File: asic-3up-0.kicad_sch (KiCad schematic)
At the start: 81 parts, among them U10 BM1362AC_MODE1, U12 MCP1824T-1202E/OT, U13 MCP1824T-0802E, U14 MCP1824T-1202E/OT, U15 MCP1824T-0802E, U4 MCP1824T-1202E/OT, U5 MCP1824T-0802E, U8 BM1362AC_MODE1, U9 BM1362AC_MODE0

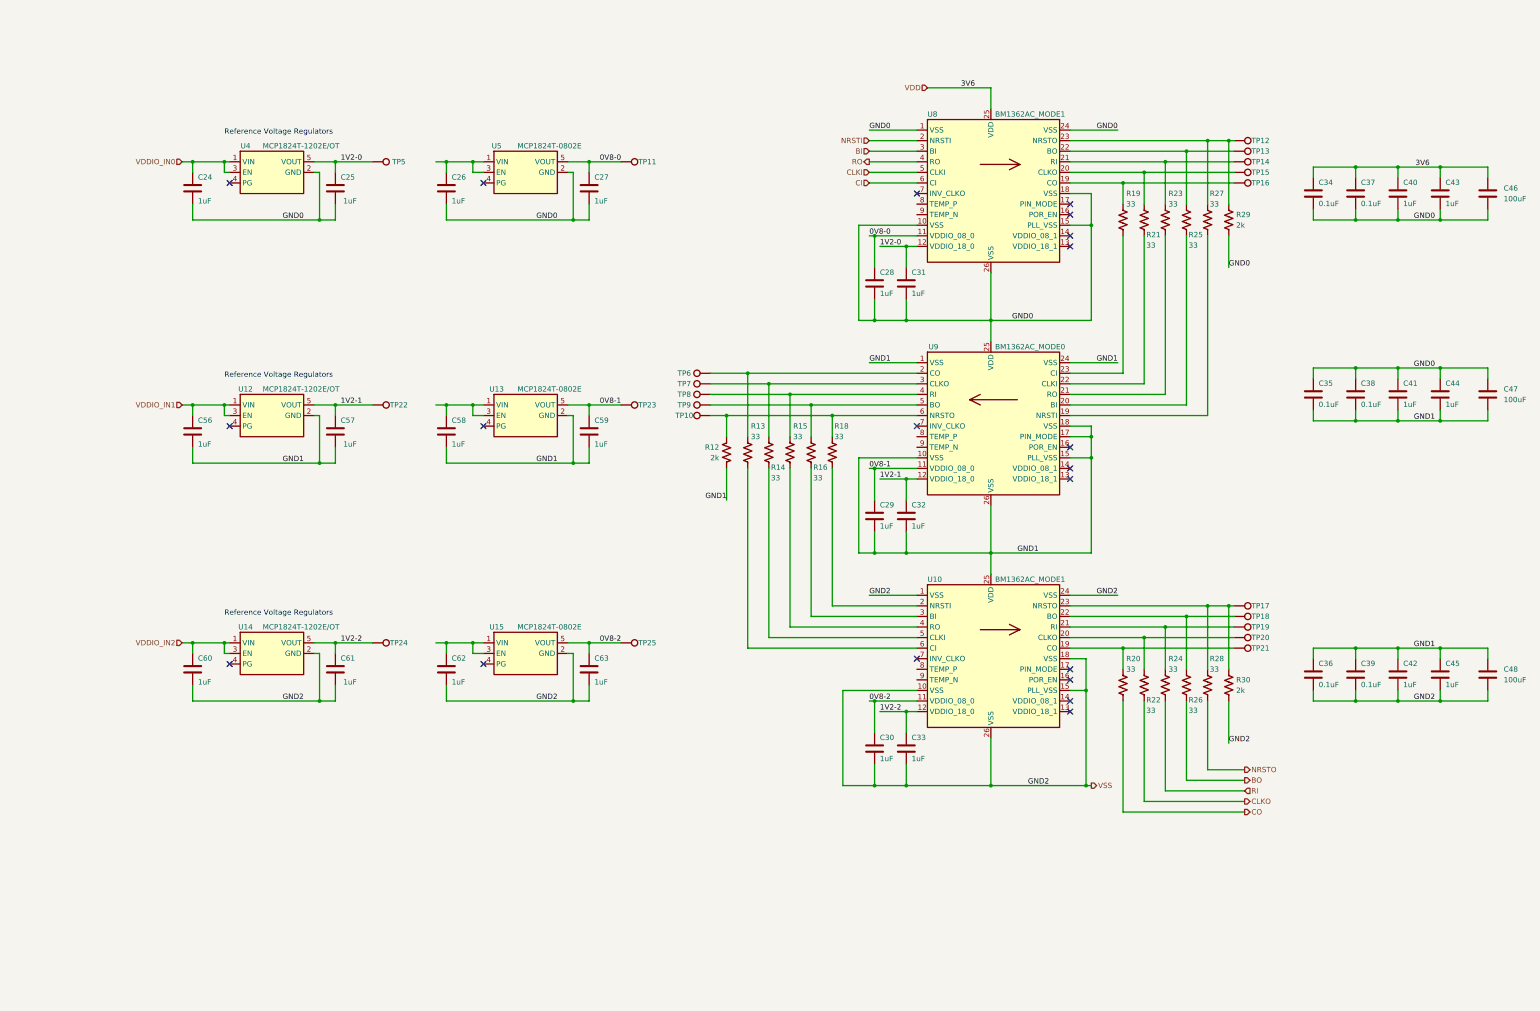
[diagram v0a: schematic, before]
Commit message: added all the ASICs to the schematic. added the RP2040 circuit for data. added the VDDIO boost circuit. schematic cleanup
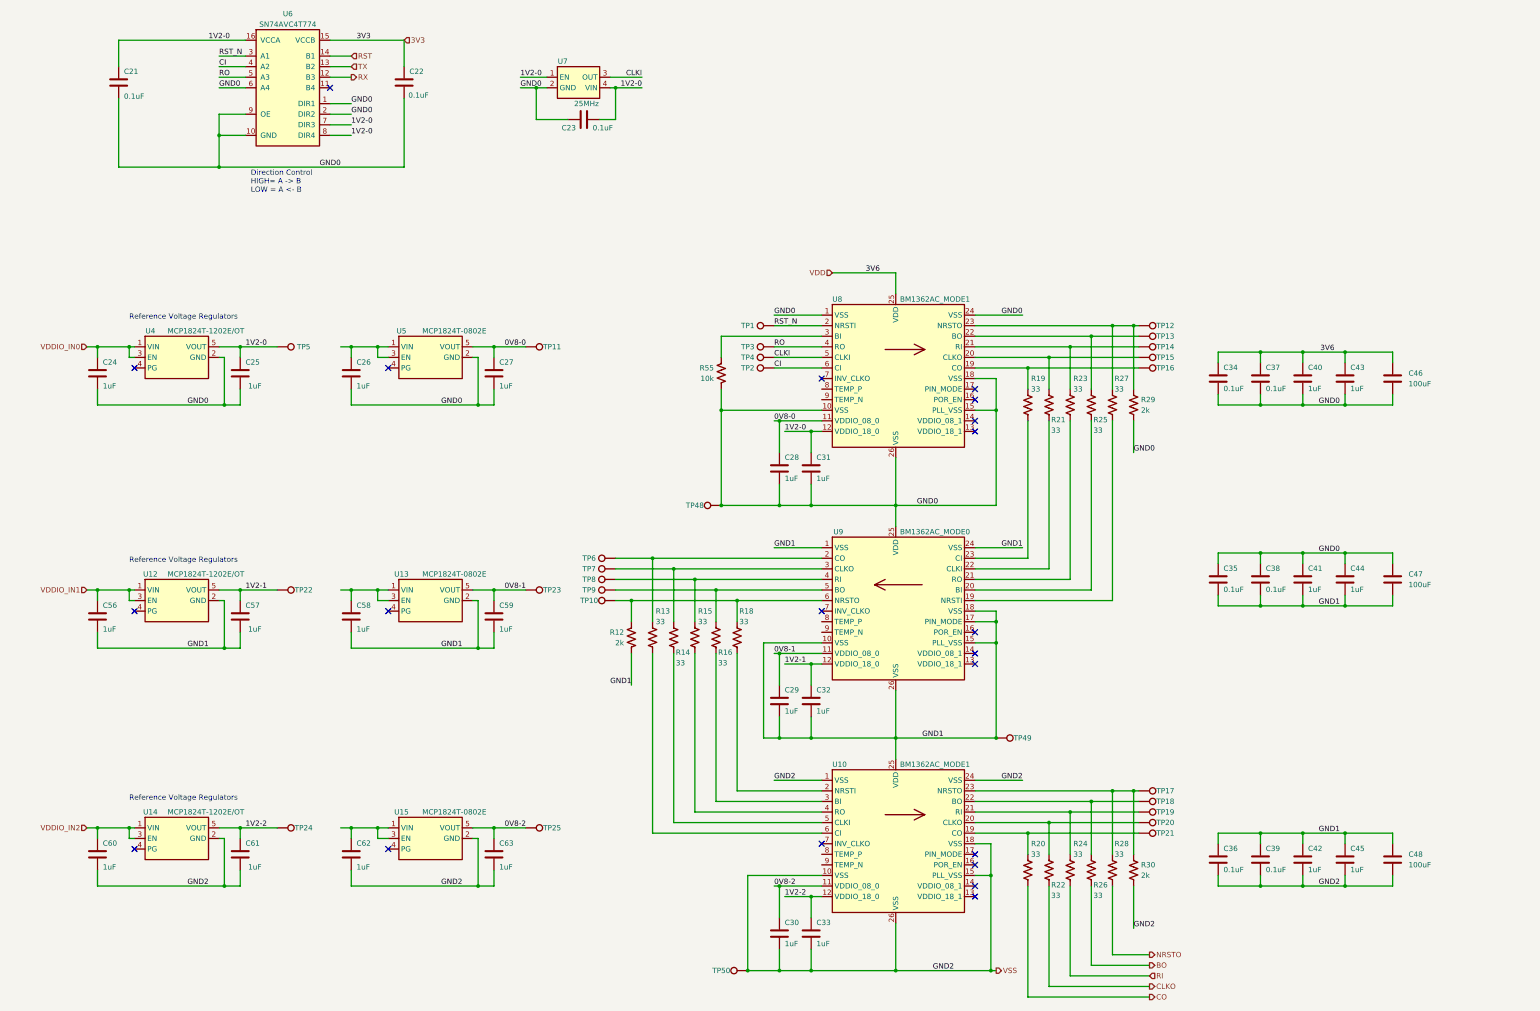
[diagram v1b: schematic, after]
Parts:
- added C21, C22, C23: 0.1uF, Capacitor_SMD:C_0402_1005Metric, symbol Device:C
- added R55: 10k, Resistor_SMD:R_0402_1005Metric, symbol Device:R_US
- added TP1, TP2, TP3, TP4, TP48, TP49, TP50: TestPoint, TestPoint:TestPoint_Pad_D1.5mm, symbol Connector:TestPoint
- added U6: SN74AVC4T774, Package_SO:TSSOP-16_4.4x5mm_P0.65mm, symbol bitaxe:SN74AVC4T774
- added U7: 25MHz, bitaxe:SMD3225-4P, symbol bitaxe:oscillator
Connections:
- net 1V2-0: now also C21.1, C23.2, U6.16 (VCCA), U6.7 (DIR3), U6.8 (DIR4), U7.1 (EN), U7.4 (VIN)
- net CI: now also TP2.1, U6.4 (A2)
- net CLKI: now also TP4.1, U7.3 (OUT)
- net GND0: now also C21.2, C22.2, C23.1, R55.2, TP48.1, U6.1 (DIR1), U6.10 (GND), U6.2 (DIR2), U6.6 (A4), U6.9 (OE), U7.2 (GND)
- net GND1: now also TP49.1
- net RO: now also TP3.1, U6.5 (A3)
- net VSS: now also TP50.1
- net BI: no longer names the net of U8.3 (BI)
- net BI: now also R55.1
- net NRSTI renamed RST_N
- net RST_N: now also TP1.1, U6.3 (A1)
- new net 3V3: C22.1, U6.15 (VCCB)
- new net RST: U6.14 (B1)
- new net RX: U6.12 (B3)
- new net TX: U6.13 (B2)
- no-connect marks 20 -> 21
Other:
- note added: "Direction Control HIGH= A -> B LOW = A <- B"
- moved on the sheet: C24, C25, C26, C27, C28, C29, C30, C31, C32, C33, C34, C35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

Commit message: added sweet logo to schematic worksheet. Schematic cleanup.
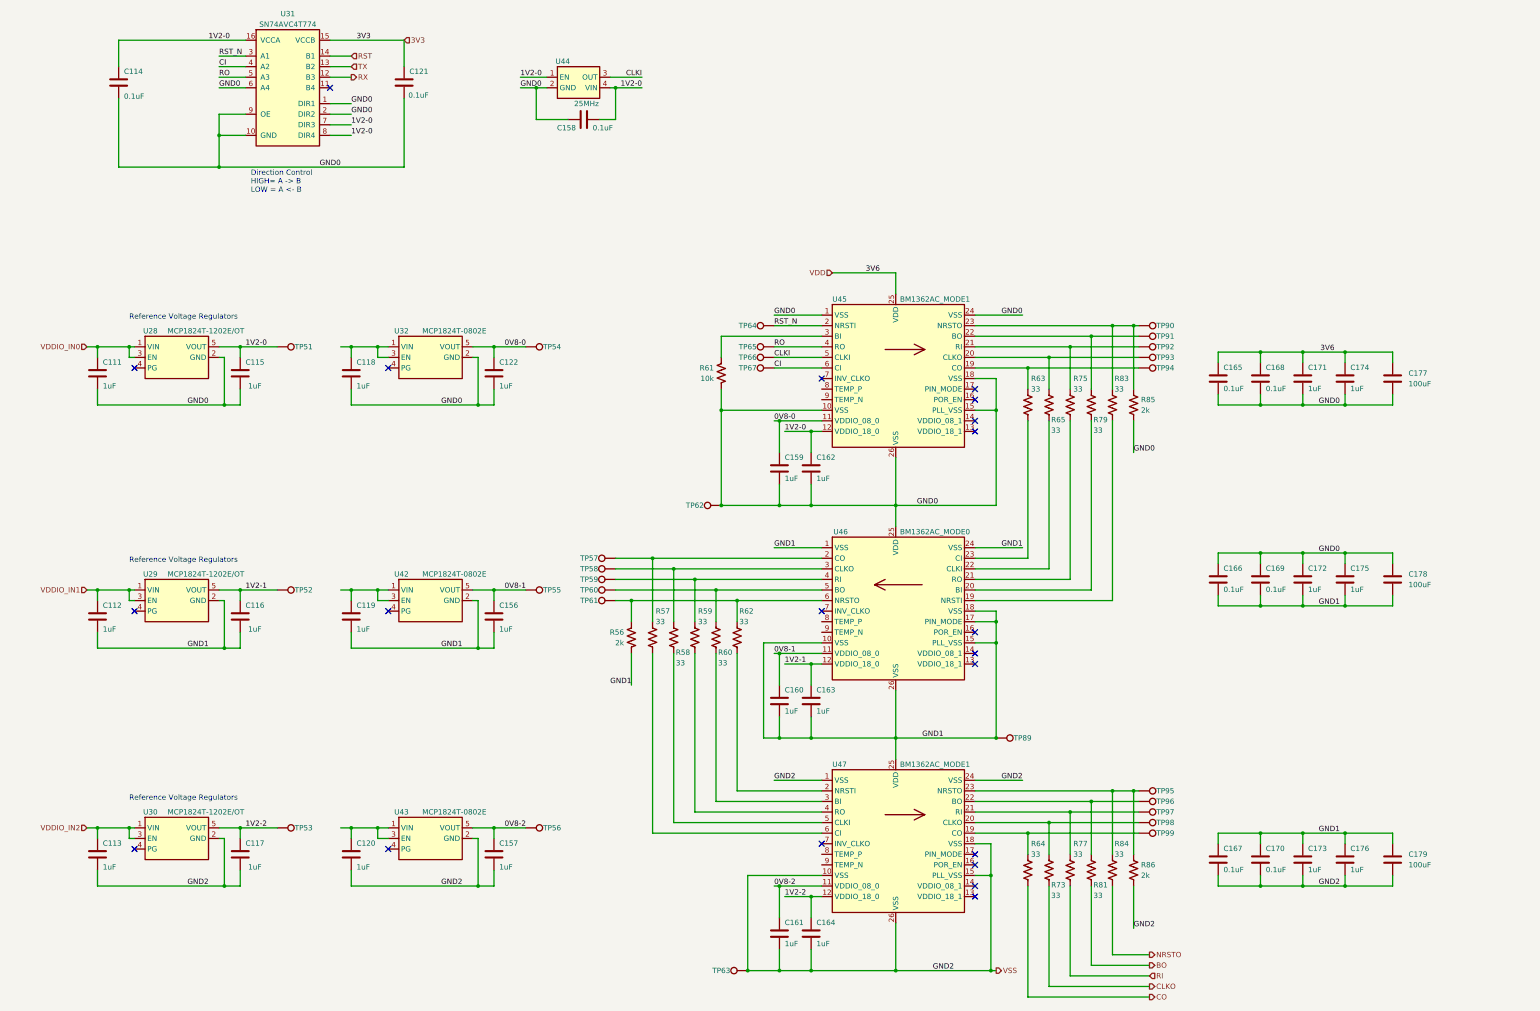
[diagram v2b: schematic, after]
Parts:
- renumbered C24 to C111, C56 to C112, C60 to C113, C21 to C114, C25 to C115, C57 to C116, C61 to C117, C26 to C118, C58 to C119, C62 to C120, C22 to C121, C27 to C122, C59 to C156, C63 to C157, C23 to C158, C28 to C159, C29 to C160, C30 to C161, C31 to C162, C32 to C163, C33 to C164, C34 to C165, C35 to C166, C36 to C167, C37 to C168, C38 to C169, C39 to C170, C40 to C171, C41 to C172, C42 to C173, C43 to C174, C44 to C175, C45 to C176, C46 to C177, C47 to C178, C48 to C179, R12 to R56, R13 to R57, R14 to R58, R15 to R59, R16 to R60, R55 to R61, R18 to R62, R19 to R63, R20 to R64, R21 to R65, R22 to R73, R23 to R75, R24 to R77, R25 to R79, R26 to R81, R27 to R83, R28 to R84, R29 to R85, R30 to R86, TP5 to TP51, TP22 to TP52, TP24 to TP53, TP11 to TP54, TP23 to TP55, TP25 to TP56, TP6 to TP57, TP7 to TP58, TP8 to TP59, TP9 to TP60, TP10 to TP61, TP48 to TP62, TP50 to TP63, TP1 to TP64, TP3 to TP65, TP4 to TP66, TP2 to TP67, TP49 to TP89, TP12 to TP90, TP13 to TP91, TP14 to TP92, TP15 to TP93, TP16 to TP94, TP17 to TP95, TP18 to TP96, TP19 to TP97, TP20 to TP98, TP21 to TP99, U4 to U28, U12 to U29, U14 to U30, U6 to U31, U5 to U32, U13 to U42, U15 to U43, U7 to U44, U8 to U45, U9 to U46, U10 to U47

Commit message: starting layout
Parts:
- added J3, J4: Conn_01x01, emberone:5x9_powertab, symbol Connector_Generic:Conn_01x01
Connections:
- net GND0: now also J3.1 (Pin_1)
- net GND1: now also J4.1 (Pin_1)
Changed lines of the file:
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@@
 	)
 	(junction
+		(at 226.06 140.97)
+		(diameter 0)
+		(color 0 0 0 0)
+	)
+	(junction
 		(at 334.01 227.33)
 		(diameter 0)
@@
 	)
 	(junction
+		(at 226.06 198.12)
+		(diameter 0)
+		(color 0 0 0 0)
+	)
+	(junction
 		(at 139.7 48.26)
 		(diameter 0)
@@
 	(wire
 		(pts
+			(xy 226.06 140.97) (xy 226.06 148.59)
+		)
+		(stroke
+			(width 0)
+			(type default)
+		)
+	)
+	(wire
+		(pts
 			(xy 68.58 168.91) (xy 77.47 168.91)
 		)
@@
 	(wire
 		(pts
+			(xy 226.06 198.12) (xy 226.06 204.47)
+		)
+		(stroke
+			(width 0)
+			(type default)
+		)
+	)
+	(wire
+		(pts
 			(xy 187.96 176.53) (xy 187.96 171.45)
 		)
@@
 	(wire
 		(pts
-			(xy 226.06 137.16) (xy 226.06 148.59)
+			(xy 226.06 137.16) (xy 226.06 140.97)
 		)
 		(stroke
@@
 	(wire
 		(pts
-			(xy 226.06 193.04) (xy 226.06 204.47)
+			(xy 226.06 193.04) (xy 226.06 198.12)
 		)
 		(stroke
@@
 	)
 	(symbol
+		(lib_id "Connector_Generic:Conn_01x01")
+		(at 231.14 198.12 0)
+		(unit 1)
+		(exclude_from_sim no)
+		(in_bom yes)
+		(on_board yes)
+		(dnp no)
+		(property "Reference" "J4"
+			(at 233.426 198.12 0)
+			(effects
+				(font
+					(size 1.27 1.27)
+				)
+				(justify left)
+			)
+		)
+		(property "Value" "Conn_01x01"
+			(at 233.68 199.3899 0)
+			(effects
+				(font
+					(size 1.27 1.27)
+				)
+				(justify left)
+				(hide yes)
+			)
+		)
+		(property "Footprint" "emberone:5x9_powertab"
+			(at 231.14 198.12 0)
+			(effects
+				(font
+					(size 1.27 1.27)
+				)
+				(hide yes)
+			)
+		)
+		(property "Datasheet" "~"
+			(at 231.14 198.12 0)
+			(effects
+				(font
+					(size 1.27 1.27)
+				)
+				(hide yes)
+			)
+		)
+		(property "Description" "powertab"
+			(at 231.14 198.12 0)
+			(effects
+				(font
+					(size 1.27 1.27)
+				)
+				(hide yes)
+			)
+		)
+		(pin "1"
+		)
+		(instances
+			(project "emberone"
+				(path "/b036224c-4cdf-48cc-81df-19bc5283ebd2/dea5684e-9ec9-4967-b9ef-d4ee852a3fa0"
+					(reference "J4")
+					(unit 1)
+				)
+			)
+		)
+	)
+	(symbol
 		(lib_id "emberone:BM1362AC_MODE1")
 		(at 226.06 116.84 0)
@@
 					(unit 1)
 				)
+			)
+		)
+	)
+	(symbol
+		(lib_id "Connector_Generic:Conn_01x01")
+		(at 231.14 140.97 0)
+		(unit 1)
+		(exclude_from_sim no)
+		(in_bom yes)
+		(on_board yes)
+		(dnp no)
+		(property "Reference" "J3"
+			(at 233.426 140.97 0)
+			(effects
+				(font
+					(size 1.27 1.27)
+				)
+				(justify left)
+			)
+		)
+		(property "Value" "Conn_01x01"
+			(at 233.68 142.2399 0)
+			(effects
+				(font
+					(size 1.27 1.27)
+				)
+				(justify left)
+				(hide yes)
+			)
+		)
+		(property "Footprint" "emberone:5x9_powertab"
+			(at 231.14 140.97 0)
+			(effects
+				(font
+					(size 1.27 1.27)
+				)
+				(hide yes)
+			)
+		)
+		(property "Datasheet" "~"
+			(at 231.14 140.97 0)
+			(effects
+				(font
+					(size 1.27 1.27)
+				)
+				(hide yes)
+			)
+		)
+		(property "Description" "powertab"
+			(at 231.14 140.97 0)
+			(effects
+				(font
+					(size 1.27 1.27)
+				)
+				(hide yes)
+			)
+		)
+		(pin "1"
+		)
+		(instances
+			(project ""
+				(path "/b036224c-4cdf-48cc-81df-19bc5283ebd2/dea5684e-9ec9-4967-b9ef-d4ee852a3fa0"
+					(reference "J3")
+					(unit 1)
+				)
